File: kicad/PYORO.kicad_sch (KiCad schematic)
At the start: 99 parts, among them J1 BM06B-SRSS-TBLFSN, J2 Conn_01x04_Pin, J3 BM06B-SRSS-TBLFSN, Q1 TEFT4300, Q2 TEFT4300, Q3 TEFT4300, Q4 TEFT4300, Q5 NMOS, Q6 NMOS, Q7 NMOS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

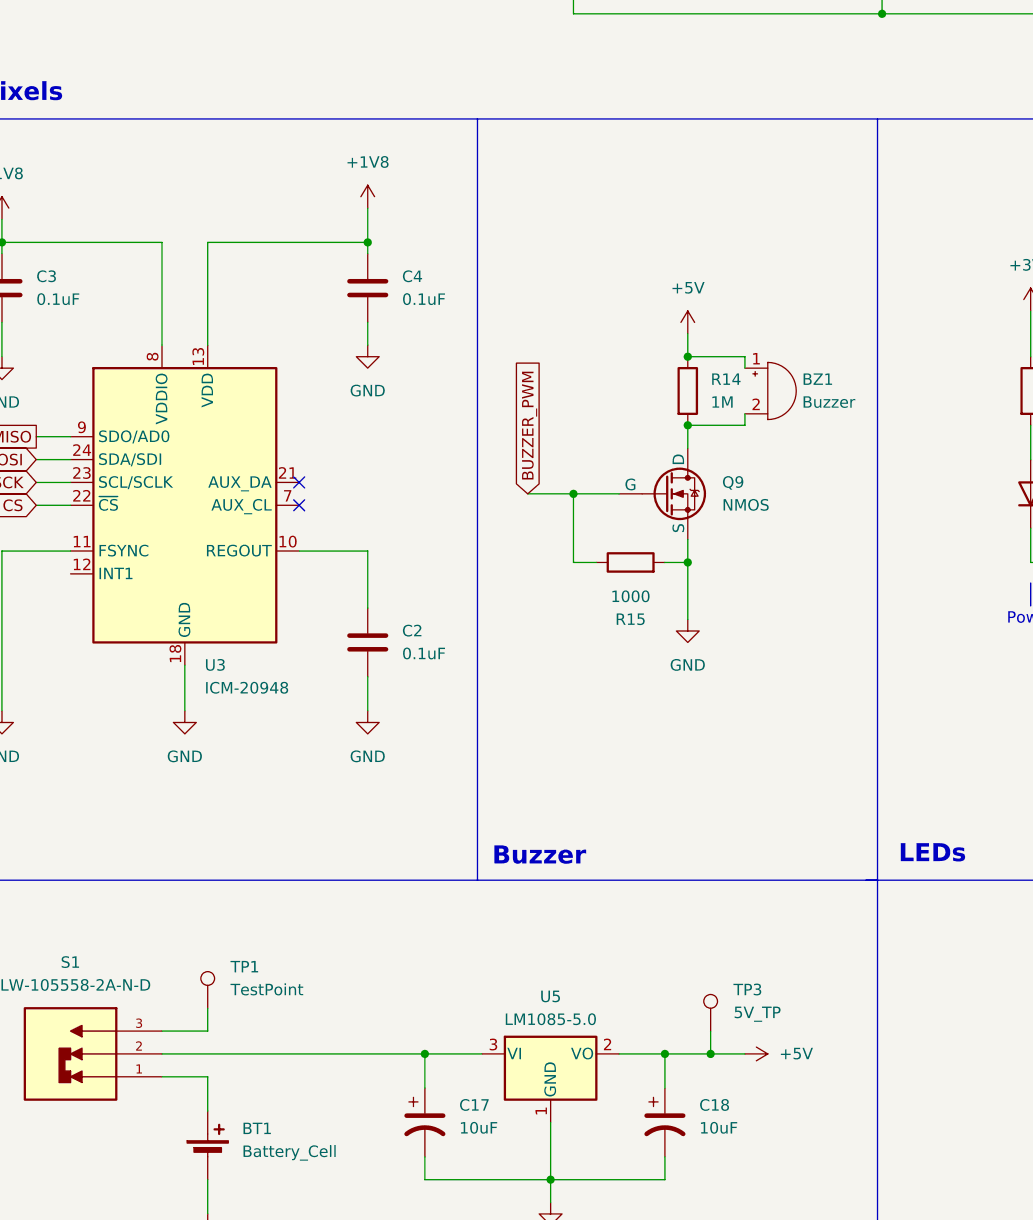
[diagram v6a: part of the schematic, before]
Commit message: Fix some schematics error, and define resistor values
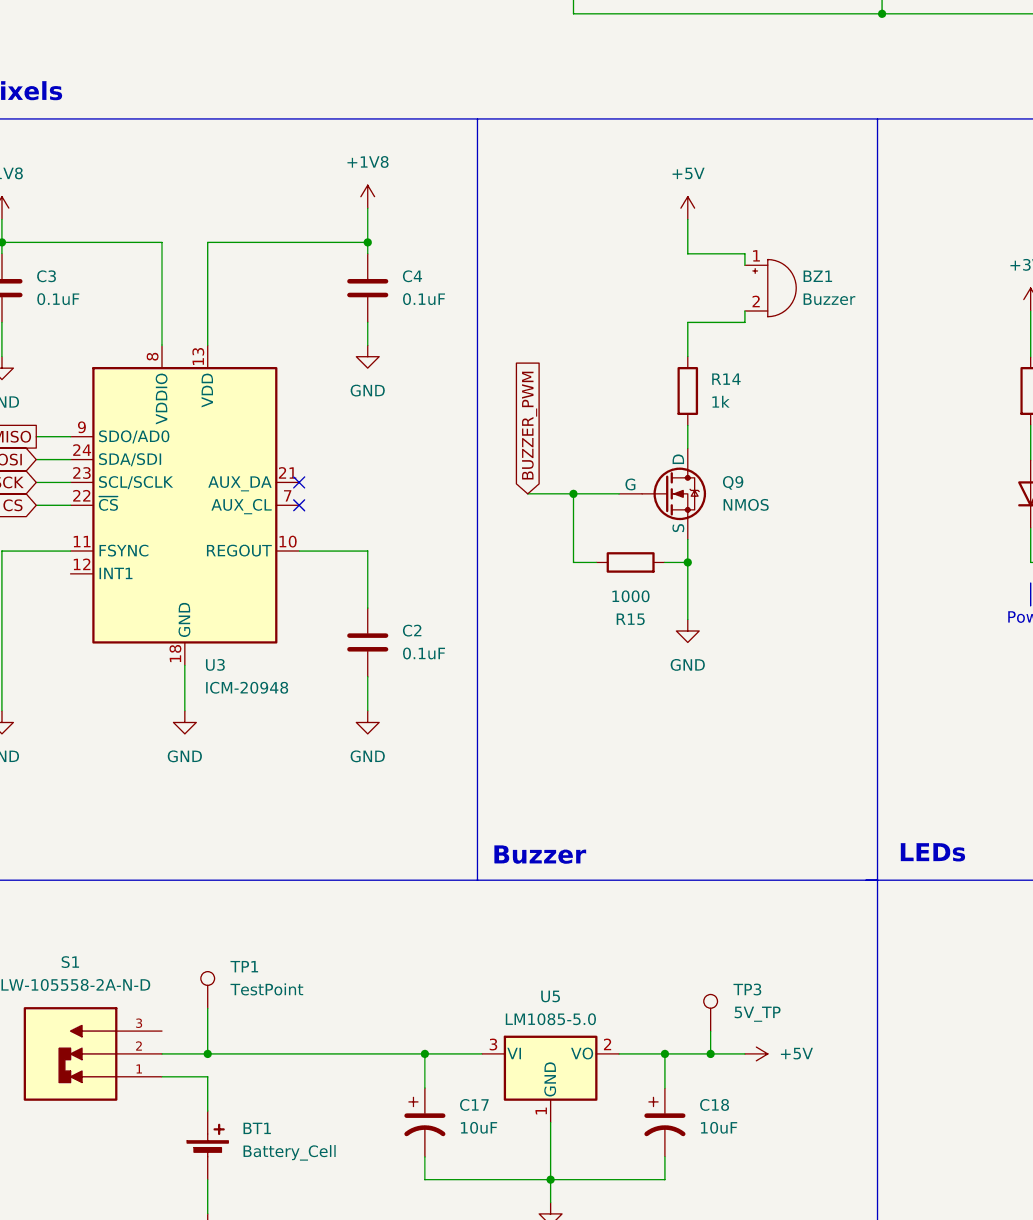
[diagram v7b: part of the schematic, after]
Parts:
- R14: value 1M -> 1k
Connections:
- net +5V: no longer R14.1
- net at Q9.1 (D), R14.2: no longer BZ1.2 (-)
- net at TP1.1: now also C17.1, S1.2, U5.3 (VI); no longer S1.3
- new net: BZ1.2 (-), R14.1
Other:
- moved on the sheet: BZ1

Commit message: Added UART support incase
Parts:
- removed C27: 4.7uF, symbol Device:C
- removed FSP-1: ~, Package_QFP:LQFP-48_7x7mm_P0.5mm, symbol FSP201:FSP201
- added J4: Conn_01x04_Pin, Connector_PinHeader_1.00mm:PinHeader_1x04_P1.00mm_Vertical, symbol Connector:Conn_01x04_Pin
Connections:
- net +5V: now also J4.1 (Pin_1)
- net GND: now also J4.4 (Pin_4)
- net UART_TX: now reaches U1.39 (PB3(JTDO)
- net UART_TX: now also J4.3 (Pin_3)
- net LED3: no longer names the net of R19.1
- net LED3: no longer U1.25 (PB12)
- new net UART_RX: J4.2 (Pin_2), U1.25 (PB12)
- no-connect marks 5 -> 7
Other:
- moved on the sheet: C21, C22, C24, J2
